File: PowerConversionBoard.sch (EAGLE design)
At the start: 48 parts, among them U1 LM2678, U2 LM2678

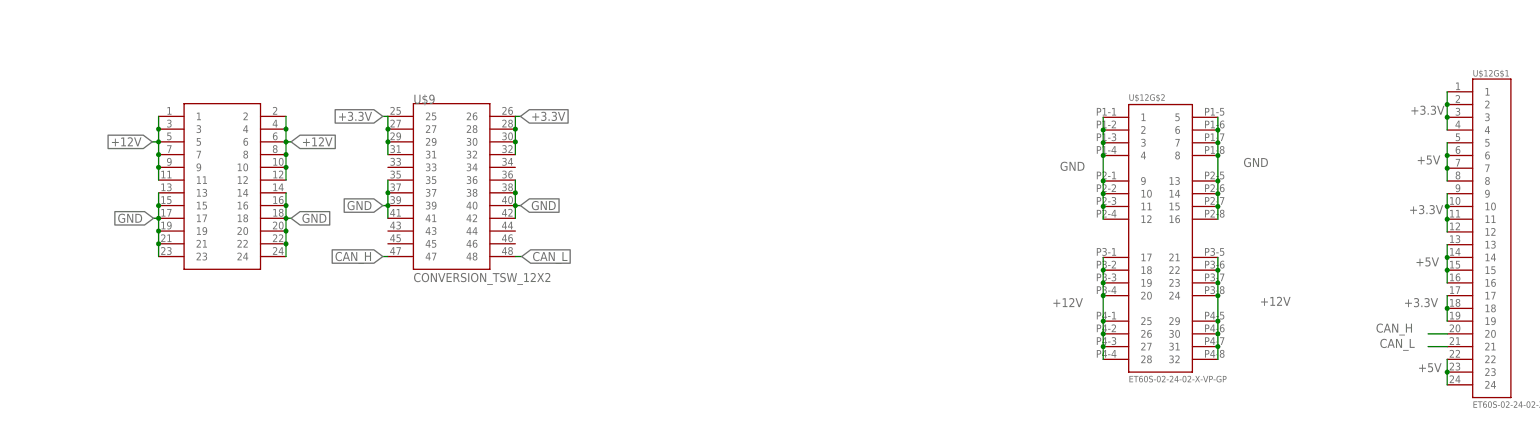
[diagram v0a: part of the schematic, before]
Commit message: CAD for connectors
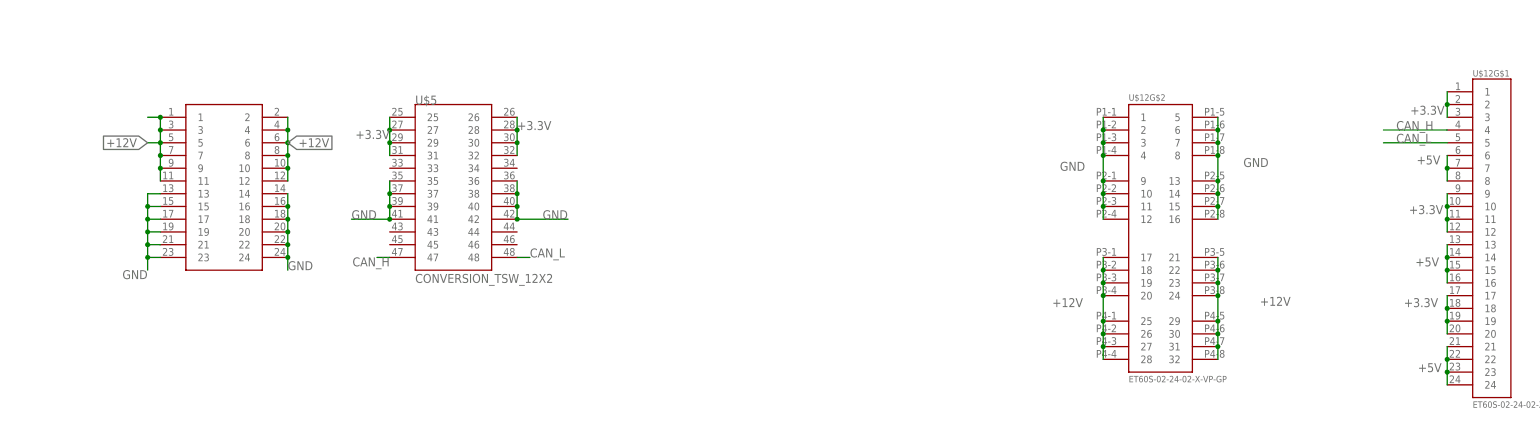
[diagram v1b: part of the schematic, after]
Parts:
- removed U$9: CONVERSION_TSW_12X2, Conversion_Connector:CONVERSION_TSW_12X2
- added U$5: CONVERSION_TSW_12X2, Dist_to_Conversion_Connector:CONVERSION_TSW_12X2
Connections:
- net +12V: now also U$5.1, U$5.10, U$5.11, U$5.12, U$5.2, U$5.3, U$5.4, U$5.5, U$5.6, U$5.7, U$5.8, U$5.9; no longer U$9.1, U$9.10, U$9.11, U$9.12, U$9.2, U$9.3, U$9.4, U$9.5, U$9.6, U$9.7, U$9.8, U$9.9
- net +3.3V: now also U$12G$1.20, U$5.25, U$5.26, U$5.27, U$5.28, U$5.29, U$5.30, U$5.31, U$5.32; no longer U$12G$1.4, U$9.25, U$9.26, U$9.27, U$9.28, U$9.29, U$9.30, U$9.31, U$9.32
- net +5V: now also U$12G$1.21; no longer U$12G$1.5
- net CAN_H: now also U$12G$1.4, U$5.47; no longer U$12G$1.20, U$9.47
- net CAN_L: now also U$12G$1.5, U$5.48; no longer U$12G$1.21, U$9.48
- net GND: now also U$5.13, U$5.14, U$5.15, U$5.16, U$5.17, U$5.18, U$5.19, U$5.20, U$5.21, U$5.22, U$5.23, U$5.24, U$5.35, U$5.36, U$5.37, U$5.38, U$5.39, U$5.40, U$5.41, U$5.42; no longer U$9.13, U$9.14, U$9.15, U$9.16, U$9.17, U$9.18, U$9.19, U$9.20, U$9.21, U$9.22, U$9.23, U$9.24, U$9.35, U$9.36, U$9.37, U$9.38, U$9.39, U$9.40, U$9.41, U$9.42

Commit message: chopped off corners
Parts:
- removed U$7: HCM1305, HCM1305:HCM1305
- added U$6: HCMA1305, Inductor_15uH - hcma1305:HCMA1305
- U$2: value HCM1305 -> HCMA1305; device HCM1305:HCM1305 -> Inductor_15uH - hcma1305:HCMA1305
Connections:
- net +5V_3.3V: now also U$6.2; no longer U$7.2
- net N$7: now also U$6.1; no longer U$7.1
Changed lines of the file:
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@@
 <part name="D3" library="SparkFun-LED" library_urn="urn:adsk.eagle:library:529" deviceset="LED" device="0603" package3d_urn="urn:adsk.eagle:package:39354/1"/>
 <part name="D4" library="SparkFun-LED" library_urn="urn:adsk.eagle:library:529" deviceset="LED" device="0603" package3d_urn="urn:adsk.eagle:package:39354/1"/>
-<part name="U$7" library="HCM1305" deviceset="HCM1305" device=""/>
-<part name="U$2" library="HCM1305" deviceset="HCM1305" device=""/>
 <part name="+12V" library="TP" deviceset="TP" device=""/>
 <part name="GND_TP" library="TP" deviceset="TP" device=""/>
@@
 <part name="U$12" library="ET60S-02-24-02-X-VP-GP" deviceset="ET60S-02-24-02-X-VP-GP" device="" package3d_urn="urn:adsk.eagle:package:23038846/2"/>
 <part name="U$5" library="Dist_to_Conversion_Connector" library_urn="urn:adsk.eagle:library:23140426" deviceset="CONVERSION_TSW_12X2" device="" package3d_urn="urn:adsk.eagle:package:23140429/2"/>
+<part name="U$2" library="Inductor_15uH - hcma1305" library_urn="urn:adsk.eagle:library:24201699" deviceset="HCMA1305" device="" package3d_urn="urn:adsk.eagle:package:24201702/1"/>
+<part name="U$6" library="Inductor_15uH - hcma1305" library_urn="urn:adsk.eagle:library:24201699" deviceset="HCMA1305" device="" package3d_urn="urn:adsk.eagle:package:24201702/1"/>
 </parts>
 <sheets>
@@
 <attribute name="VALUE" x="307.975" y="69.85" size="1.778" layer="96" font="vector" rot="R90" align="top-left"/>
 </instance>
-<instance part="U$7" gate="G$1" x="476.758" y="66.04" smashed="yes" rot="R90">
-<attribute name="NAME" x="471.66238125" y="68.587809375" size="1.78346875" layer="95"/>
-</instance>
-<instance part="U$2" gate="G$1" x="90.932" y="55.372" smashed="yes" rot="R90">
-<attribute name="NAME" x="85.83638125" y="57.919809375" size="1.78346875" layer="95"/>
-</instance>
 <instance part="+12V" gate="G$1" x="-71.628" y="14.478" smashed="yes" rot="R270">
 <attribute name="NAME" x="-69.088" y="12.7" size="1.778" layer="95" rot="R270"/>
@@
 <attribute name="NAME" x="-12.7" y="-203.2" size="1.778" layer="95"/>
 <attribute name="VALUE" x="-12.7" y="-238.76" size="1.778" layer="96"/>
+</instance>
+<instance part="U$2" gate="G$1" x="91.44" y="55.88" smashed="yes" rot="R90">
+<attribute name="NAME" x="85.09" y="58.42" size="1.778" layer="95" rot="R90"/>
+<attribute name="VALUE" x="97.79" y="58.42" size="1.778" layer="96" rot="R90"/>
+</instance>
+<instance part="U$6" gate="G$1" x="477.52" y="66.04" smashed="yes" rot="R90">
+<attribute name="NAME" x="471.17" y="68.58" size="1.778" layer="95" rot="R90"/>
+<attribute name="VALUE" x="483.87" y="68.58" size="1.778" layer="96" rot="R90"/>
 </instance>
 </instances>
@@
 <net name="+5V" class="0">
 <segment>
-<wire x1="103.632" y1="55.372" x2="106.172" y2="55.372" width="0.1524" layer="91"/>
+<wire x1="104.14" y1="55.88" x2="106.172" y2="55.372" width="0.1524" layer="91"/>
 <wire x1="106.172" y1="55.372" x2="118.872" y2="55.372" width="0.1524" layer="91"/>
 <wire x1="118.872" y1="55.372" x2="131.572" y2="55.372" width="0.1524" layer="91"/>
-<wire x1="98.552" y1="55.372" x2="103.632" y2="55.372" width="0.1524" layer="91"/>
-<junction x="103.632" y="55.372"/>
+<wire x1="99.06" y1="55.88" x2="104.14" y2="55.88" width="0.1524" layer="91"/>
+<junction x="104.14" y="55.88"/>
 <pinref part="P+1" gate="1" pin="+5V"/>
 <wire x1="103.632" y1="73.152" x2="103.632" y2="65.532" width="0.1524" layer="91"/>
 <pinref part="U1" gate="G$1" pin="FEEDBACK"/>
-<wire x1="103.632" y1="65.532" x2="103.632" y2="55.372" width="0.1524" layer="91"/>
+<wire x1="103.632" y1="65.532" x2="104.14" y2="55.88" width="0.1524" layer="91"/>
 <wire x1="60.452" y1="65.532" x2="103.632" y2="65.532" width="0.1524" layer="91"/>
 <junction x="103.632" y="65.532"/>
@@
 <wire x1="458.978" y1="71.12" x2="464.058" y2="71.12" width="0.1524" layer="91"/>
 <wire x1="464.058" y1="71.12" x2="464.058" y2="66.04" width="0.1524" layer="91"/>
-<wire x1="469.138" y1="66.04" x2="464.058" y2="66.04" width="0.1524" layer="91"/>
+<wire x1="469.138" y1="66.04" x2="467.36" y2="66.04" width="0.1524" layer="91"/>
 <junction x="464.058" y="66.04"/>
 <pinref part="U$3" gate="G$1" pin="P$4"/>
+<wire x1="467.36" y1="66.04" x2="464.058" y2="66.04" width="0.1524" layer="91"/>
 <wire x1="461.518" y1="66.04" x2="464.058" y2="66.04" width="0.1524" layer="91"/>
 <wire x1="461.518" y1="60.96" x2="461.518" y2="66.04" width="0.1524" layer="91"/>
 <junction x="461.518" y="66.04"/>
-<pinref part="U$7" gate="G$1" pin="1"/>
+<pinref part="U$6" gate="G$1" pin="1"/>
+<wire x1="469.9" y1="66.04" x2="469.138" y2="66.04" width="0.1524" layer="91"/>
 </segment>
 </net>
@@
 <wire x1="489.458" y1="66.04" x2="502.158" y2="66.04" width="0.1524" layer="91"/>
 <wire x1="502.158" y1="66.04" x2="514.858" y2="66.04" width="0.1524" layer="91"/>
-<wire x1="484.378" y1="66.04" x2="489.458" y2="66.04" width="0.1524" layer="91"/>
+<wire x1="484.378" y1="66.04" x2="485.14" y2="66.04" width="0.1524" layer="91"/>
 <junction x="489.458" y="66.04"/>
 <pinref part="U2" gate="G$1" pin="FEEDBACK"/>
+<wire x1="485.14" y1="66.04" x2="489.458" y2="66.04" width="0.1524" layer="91"/>
 <wire x1="489.458" y1="76.2" x2="489.458" y2="66.04" width="0.1524" layer="91"/>
 <wire x1="446.278" y1="76.2" x2="489.458" y2="76.2" width="0.1524" layer="91"/>
@@
 <label x="489.458" y="83.82" size="1.778" layer="95" rot="R90" xref="yes"/>
 <wire x1="489.458" y1="76.2" x2="489.458" y2="83.82" width="0.1524" layer="91"/>
-<pinref part="U$7" gate="G$1" pin="2"/>
+<pinref part="U$6" gate="G$1" pin="2"/>
+<junction x="485.14" y="66.04"/>
 </segment>
 <segment>
@@
 <pinref part="C6" gate="G$1" pin="2"/>
 <wire x1="73.152" y1="60.452" x2="78.232" y2="60.452" width="0.1524" layer="91"/>
-<wire x1="78.232" y1="60.452" x2="78.232" y2="55.372" width="0.1524" layer="91"/>
-<wire x1="83.312" y1="55.372" x2="78.232" y2="55.372" width="0.1524" layer="91"/>
-<junction x="78.232" y="55.372"/>
+<wire x1="78.232" y1="60.452" x2="78.74" y2="55.88" width="0.1524" layer="91"/>
 <pinref part="U$1" gate="G$1" pin="P$4"/>
-<wire x1="75.692" y1="55.372" x2="78.232" y2="55.372" width="0.1524" layer="91"/>
+<wire x1="75.692" y1="55.372" x2="78.74" y2="55.88" width="0.1524" layer="91"/>
 <wire x1="75.692" y1="50.292" x2="75.692" y2="55.372" width="0.1524" layer="91"/>
 <junction x="75.692" y="55.372"/>
 <pinref part="U$2" gate="G$1" pin="1"/>
+<wire x1="83.82" y1="55.88" x2="78.74" y2="55.88" width="0.1524" layer="91"/>
+<junction x="78.74" y="55.88"/>
 </segment>
 </net>

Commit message: stupid outline. extra breakouts. tighter layout.
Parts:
- removed +12V, +3.3, 5V, 5V_3.3_TP, GND_TP: TP, TP:TP
- removed 12V: (no value), SparkFun-Connectors:BANANA_CONN
- added J1: (no value), SparkFun-Connectors:CONN_01
- added J2, J7: (no value), SparkFun-Connectors:CONN_02
- added J3, J4, J5, J6: (no value), SparkFun-Connectors:CONN_04
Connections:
- net N$1 renamed SW_5
- net N$2 renamed BST_5_3
- net N$3 renamed BST
- net N$7 renamed SW_5_3
- net +12V: now also J1.1; no longer +12V.P$1, 12V.1
- net +3.3V: now also J7.1, J7.2; no longer +3.3.P$1
- net +5V: now also J3.3, J3.4, J4.3, J4.4, J5.3, J5.4, J6.1, J6.2, J6.3, J6.4; no longer 5V.P$1
- net +5V_3.3V: no longer 5V_3.3_TP.P$1
- net CAN_H: now also J2.2
- net CAN_L: now also J2.1
- net GND: now also J3.1, J3.2, J4.1, J4.2, J5.1, J5.2; no longer GND_TP.P$1
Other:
- note removed: "Test Points"
- moved on the sheet: GND3

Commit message: added resistors for adjustable and re aligned schematic
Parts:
- removed U$2, U$6: HCMA1305, Inductor_15uH - hcma1305:HCMA1305
- added L1, L2: 15uH, Inductor_15uH - hcma1305:HCMA1305
- added R6: 10k, SparkFun-Resistors:10KOHM-0603-1/10W-1%
- added R7: 33k, SparkFun-Resistors:33KOHM-0603-1/10W-1%
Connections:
- new net FB: R6.2, R7.1, U1.FEEDBACK
- net +5V: now also L1.2, R7.2; no longer U$2.2, U1.FEEDBACK
- net +5V_3.3V: now also L2.2; no longer U$6.2
- net GND: now also R6.1
- net SW_5: now also L1.1; no longer U$2.1
- net SW_5_3: now also L2.1; no longer U$6.1
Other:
- note added: "Vfb = 1.21 Vout = 5.2 Vfb = Vout * R6 / (R6 + R7) R6 = R7(Vout / Vfb - 1) R7 = 10k R6 = 33k"
- moved on the sheet: +3.3V, +5V, 5V_3.3, C10, C11, C12, C14, C15, C16, C17, C18, C20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
